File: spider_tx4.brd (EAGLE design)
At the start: 15.4 x 30.5 mm, 6 parts, among them J1 AVR_SPI_PRG_6NS

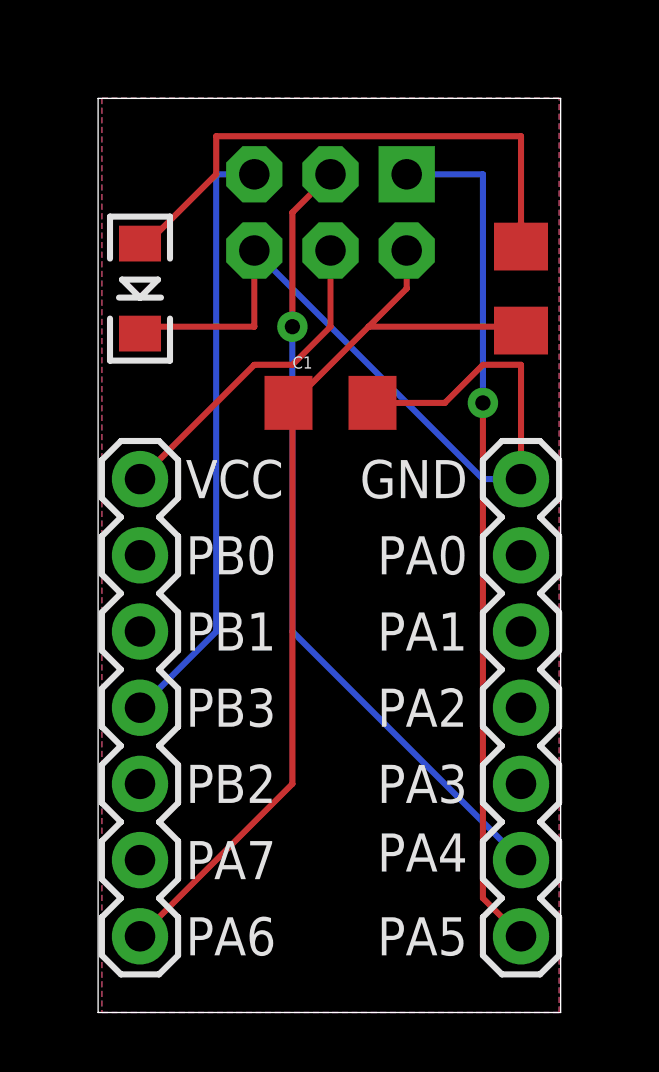
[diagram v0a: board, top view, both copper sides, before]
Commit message: noticed bug in board spidertx4.  fixed.  still tweaking.
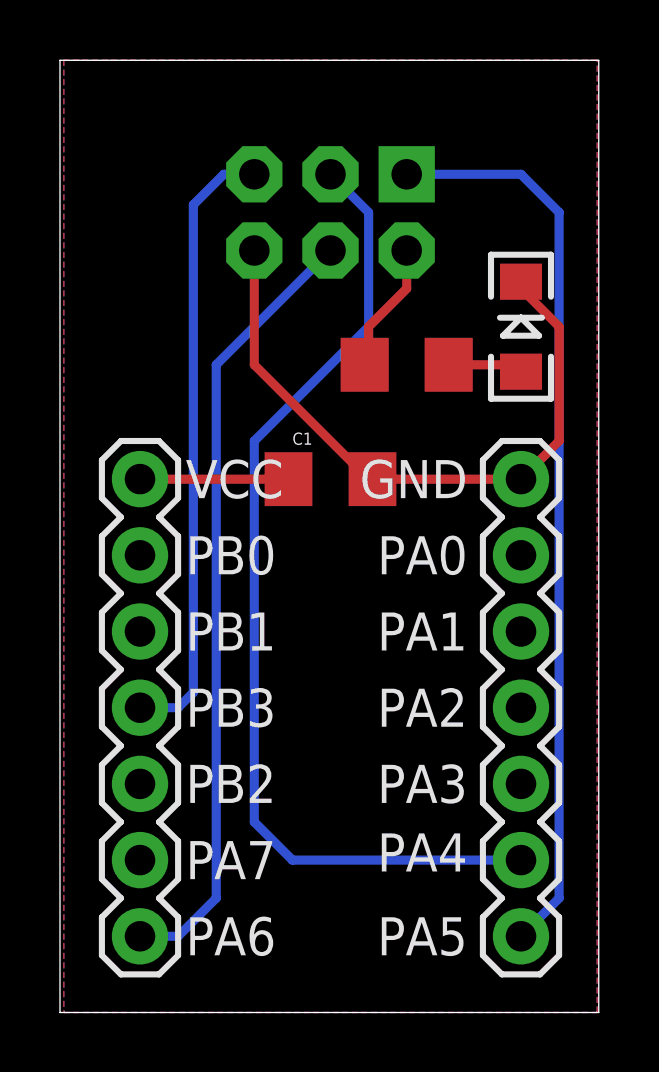
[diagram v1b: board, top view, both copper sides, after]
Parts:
- moved LEFT 15.2 mm to (2.54, 2.54), turned to 90 degrees
- moved D1 12.8 mm to (15.2, 22.9), turned to 90 degrees
- moved R1 4.58 mm to (11.4, 21.6), turned to 0 degrees
- moved C1 2.54 mm to (8.89, 17.8)
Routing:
- net VCC: track 31.9 -> 9.62 mm
- net N$14: track 19.1 -> 2.51 mm
- net MOSI: track 11.0 -> 26.2 mm
- net SCK: track 26.5 -> 33.1 mm, vias 1 -> 0
- net GND: track 28.0 -> 21.9 mm
- net MISO: track 28.5 -> 30.3 mm, vias 1 -> 0
- net RESET: track 20.1 -> 20.7 mm
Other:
- board size 15.4 x 30.5 mm -> 18 x 31.7 mm

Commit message: tweaked tx4 spider to death.  printing and testing.
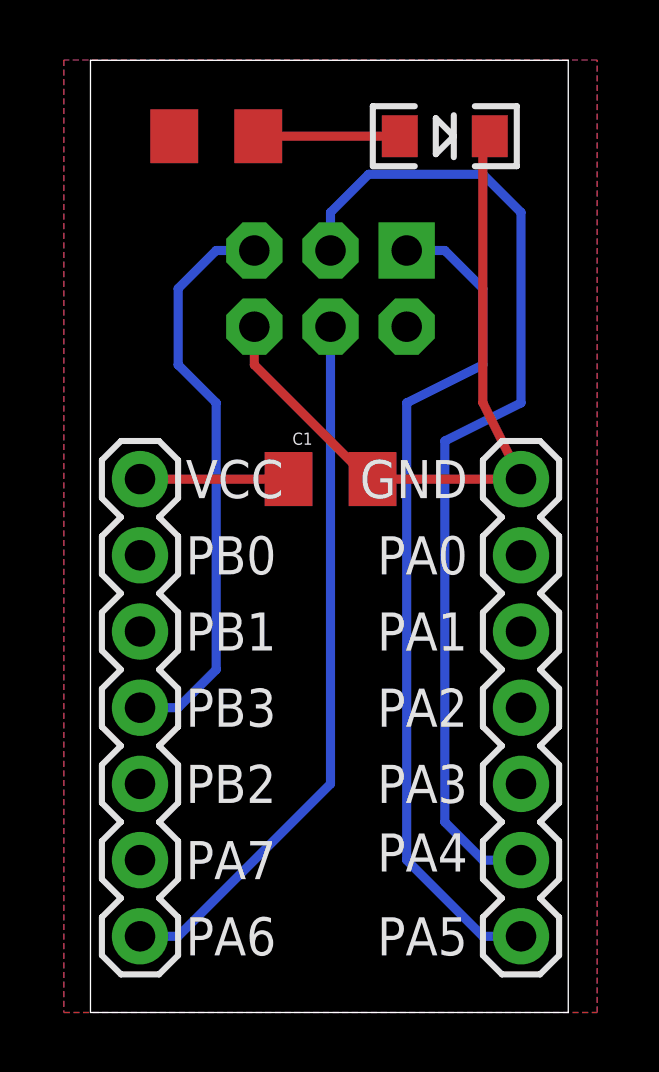
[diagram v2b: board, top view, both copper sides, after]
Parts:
- moved R1 9.92 mm to (5.08, 29.2)
- moved D1 6.84 mm to (12.7, 29.2), turned to 0 degrees
- moved J1 2.54 mm to (8.89, 24.1)
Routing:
- net VCC: track 9.62 -> 4.95 mm
- net N$14: track 2.51 -> 5.08 mm
- net MOSI: track 26.2 -> 23.7 mm
- net GND: track 21.9 -> 23.7 mm
- net MISO: track 30.3 -> 28.5 mm
- net RESET: track 20.7 -> 19.4 mm
- net SCK: track 33.1 -> 33.6 mm
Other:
- board size 18 x 31.7 mm -> 15.9 x 31.7 mm
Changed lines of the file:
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@@
 <board>
 <plain>
-<wire x1="-0.127" y1="0" x2="17.831" y2="0" width="0" layer="20"/>
-<wire x1="17.831" y1="0" x2="17.831" y2="31.74" width="0" layer="20"/>
-<wire x1="17.831" y1="31.74" x2="-0.127" y2="31.74" width="0" layer="20"/>
-<wire x1="-0.127" y1="31.74" x2="-0.127" y2="0" width="0" layer="20"/>
+<wire x1="0.889" y1="0" x2="16.815" y2="0" width="0" layer="20"/>
+<wire x1="16.815" y1="0" x2="16.815" y2="31.74" width="0" layer="20"/>
+<wire x1="16.815" y1="31.74" x2="0.889" y2="31.74" width="0" layer="20"/>
+<wire x1="0.889" y1="31.74" x2="0.889" y2="0" width="0" layer="20"/>
 <text x="13.462" y="17.78" size="1.27" layer="25" align="center-right">GND</text>
 <text x="13.462" y="15.24" size="1.27" layer="25" align="center-right">PA0</text>
@@
 </autorouter>
 <elements>
-<element name="J1" library="SparkFun-Connectors" package="2X3-NS" value="AVR_SPI_PRG_6NS" x="8.89" y="26.67" smashed="yes" rot="R180"/>
-<element name="R1" library="SparkFun-Passives" package="1206" value="1k Ohm" x="11.43" y="21.59" smashed="yes">
-<attribute name="VALUE" x="10.541" y="23.114" size="0.4064" layer="27"/>
+<element name="J1" library="SparkFun-Connectors" package="2X3-NS" value="AVR_SPI_PRG_6NS" x="8.89" y="24.13" smashed="yes" rot="R180"/>
+<element name="R1" library="SparkFun-Passives" package="1206" value="1k Ohm" x="5.08" y="29.21" smashed="yes">
+<attribute name="VALUE" x="4.191" y="30.734" size="0.4064" layer="27"/>
 </element>
-<element name="D1" library="SparkFun-LED" package="LED-1206" value="Yellow" x="15.24" y="22.86" smashed="yes" rot="R90">
-<attribute name="PROD_ID" value="DIO-09909" x="38.1" y="38.1" size="1.778" layer="27" rot="R90" display="off"/>
-<attribute name="VALUE" x="13.716" y="22.098" size="0.4064" layer="27" rot="R90"/>
+<element name="D1" library="SparkFun-LED" package="LED-1206" value="Yellow" x="12.7" y="29.21" smashed="yes">
+<attribute name="PROD_ID" value="DIO-09909" x="27.94" y="6.35" size="1.778" layer="27" display="off"/>
+<attribute name="VALUE" x="11.938" y="30.734" size="0.4064" layer="27"/>
 </element>
 <element name="C1" library="SparkFun-Passives" package="1206" value="0.1uF" x="8.89" y="17.78"/>
@@
 <contactref element="J1" pad="3"/>
 <contactref element="RIGHT" pad="6"/>
-<wire x1="8.89" y1="27.94" x2="10.16" y2="26.67" width="0.3048" layer="16"/>
-<wire x1="10.16" y1="26.67" x2="10.16" y2="22.86" width="0.3048" layer="16"/>
-<wire x1="10.16" y1="22.86" x2="6.35" y2="19.05" width="0.3048" layer="16"/>
-<wire x1="6.35" y1="19.05" x2="6.35" y2="6.35" width="0.3048" layer="16"/>
-<wire x1="6.35" y1="6.35" x2="7.62" y2="5.08" width="0.3048" layer="16"/>
-<wire x1="7.62" y1="5.08" x2="15.24" y2="5.08" width="0.3048" layer="16"/>
+<wire x1="13.97" y1="5.08" x2="15.24" y2="5.08" width="0.3048" layer="16"/>
+<wire x1="8.89" y1="25.4" x2="8.89" y2="26.67" width="0.3048" layer="16"/>
+<wire x1="8.89" y1="26.67" x2="10.16" y2="27.94" width="0.3048" layer="16"/>
+<wire x1="10.16" y1="27.94" x2="13.97" y2="27.94" width="0.3048" layer="16"/>
+<wire x1="13.97" y1="27.94" x2="15.24" y2="26.67" width="0.3048" layer="16"/>
+<wire x1="15.24" y1="26.67" x2="15.24" y2="20.32" width="0.3048" layer="16"/>
+<wire x1="15.24" y1="20.32" x2="12.7" y2="19.05" width="0.3048" layer="16"/>
+<wire x1="12.7" y1="19.05" x2="12.7" y2="6.35" width="0.3048" layer="16"/>
+<wire x1="12.7" y1="6.35" x2="13.97" y2="5.08" width="0.3048" layer="16"/>
 </signal>
 <signal name="MISO">
 <contactref element="J1" pad="1"/>
 <contactref element="RIGHT" pad="7"/>
-<wire x1="15.24" y1="2.54" x2="16.51" y2="3.81" width="0.3048" layer="16"/>
-<wire x1="16.51" y1="3.81" x2="16.51" y2="26.67" width="0.3048" layer="16"/>
-<wire x1="16.51" y1="26.67" x2="15.24" y2="27.94" width="0.3048" layer="16"/>
-<wire x1="15.24" y1="27.94" x2="11.43" y2="27.94" width="0.3048" layer="16"/>
+<wire x1="13.97" y1="2.54" x2="15.24" y2="2.54" width="0.3048" layer="16"/>
+<wire x1="11.43" y1="5.08" x2="13.97" y2="2.54" width="0.3048" layer="16"/>
+<wire x1="11.43" y1="20.32" x2="11.43" y2="5.08" width="0.3048" layer="16"/>
+<wire x1="13.97" y1="21.59" x2="11.43" y2="20.32" width="0.3048" layer="16"/>
+<wire x1="13.97" y1="21.59" x2="13.97" y2="24.13" width="0.3048" layer="16"/>
+<wire x1="13.97" y1="24.13" x2="12.7" y2="25.4" width="0.3048" layer="16"/>
+<wire x1="12.7" y1="25.4" x2="11.43" y2="25.4" width="0.3048" layer="16"/>
 </signal>
 <signal name="MOSI">
 <contactref element="J1" pad="4"/>
 <contactref element="LEFT" pad="1"/>
-<wire x1="8.89" y1="25.4" x2="5.08" y2="21.59" width="0.3048" layer="16"/>
-<wire x1="5.08" y1="21.59" x2="5.08" y2="3.81" width="0.3048" layer="16"/>
-<wire x1="5.08" y1="3.81" x2="3.81" y2="2.54" width="0.3048" layer="16"/>
 <wire x1="3.81" y1="2.54" x2="2.54" y2="2.54" width="0.3048" layer="16"/>
+<wire x1="8.89" y1="7.62" x2="3.81" y2="2.54" width="0.3048" layer="16"/>
+<wire x1="8.89" y1="22.86" x2="8.89" y2="7.62" width="0.3048" layer="16"/>
 </signal>
 <signal name="RESET">
 <contactref element="J1" pad="5"/>
 <contactref element="LEFT" pad="4"/>
-<wire x1="6.35" y1="27.94" x2="5.334" y2="27.94" width="0.3048" layer="16"/>
-<wire x1="5.334" y1="27.94" x2="4.318" y2="26.924" width="0.3048" layer="16"/>
-<wire x1="4.318" y1="26.924" x2="4.318" y2="10.668" width="0.3048" layer="16"/>
-<wire x1="4.318" y1="10.668" x2="3.81" y2="10.16" width="0.3048" layer="16"/>
 <wire x1="3.81" y1="10.16" x2="2.54" y2="10.16" width="0.3048" layer="16"/>
+<wire x1="5.08" y1="11.43" x2="3.81" y2="10.16" width="0.3048" layer="16"/>
+<wire x1="5.08" y1="20.32" x2="5.08" y2="11.43" width="0.3048" layer="16"/>
+<wire x1="5.08" y1="25.4" x2="3.81" y2="24.13" width="0.3048" layer="16"/>
+<wire x1="6.35" y1="25.4" x2="5.08" y2="25.4" width="0.3048" layer="16"/>
+<wire x1="3.81" y1="24.13" x2="3.81" y2="21.59" width="0.3048" layer="16"/>
+<wire x1="3.81" y1="21.59" x2="5.08" y2="20.32" width="0.3048" layer="16"/>
 </signal>
 <signal name="VCC">
@@
 <contactref element="LEFT" pad="7"/>
 <wire x1="2.54" y1="17.78" x2="7.49" y2="17.78" width="0.3048" layer="1"/>
-<wire x1="11.43" y1="25.4" x2="11.43" y2="24.13" width="0.3048" layer="1"/>
-<wire x1="11.43" y1="24.13" x2="10.16" y2="22.86" width="0.3048" layer="1"/>
-<wire x1="10.16" y1="22.86" x2="10.16" y2="21.72" width="0.3048" layer="1"/>
-<wire x1="10.16" y1="21.72" x2="10.03" y2="21.59" width="0.3048" layer="1"/>
 <polygon width="0.3048" layer="1">
 <vertex x="0" y="31.75"/>
@@
 <vertex x="17.78" y="31.75"/>
 </polygon>
-<wire x1="10.16" y1="21.59" x2="10.03" y2="21.59" width="0.3048" layer="1"/>
-<wire x1="10.16" y1="21.59" x2="10.182390625" y2="21.742409375" width="0.3048" layer="1"/>
 </signal>
 <signal name="GND">
@@
 </polygon>
 <wire x1="15.24" y1="17.78" x2="10.29" y2="17.78" width="0.3048" layer="1"/>
-<wire x1="6.35" y1="25.4" x2="6.35" y2="21.59" width="0.3048" layer="1"/>
+<wire x1="6.35" y1="22.86" x2="6.35" y2="21.59" width="0.3048" layer="1"/>
 <wire x1="6.35" y1="21.59" x2="10.16" y2="17.78" width="0.3048" layer="1"/>
 <wire x1="10.16" y1="17.78" x2="10.29" y2="17.78" width="0.3048" layer="1"/>
-<wire x1="16.51" y1="22.86" x2="15.24" y2="24.13" width="0.3048" layer="1"/>
-<wire x1="16.51" y1="19.05" x2="16.51" y2="22.86" width="0.3048" layer="1"/>
-<wire x1="15.24" y1="17.78" x2="16.51" y2="19.05" width="0.3048" layer="1"/>
-<wire x1="15.24" y1="24.13" x2="15.24" y2="24.36" width="0.3048" layer="1"/>
+<wire x1="13.97" y1="20.32" x2="13.97" y2="29.21" width="0.3048" layer="1"/>
+<wire x1="15.24" y1="17.78" x2="13.97" y2="20.32" width="0.3048" layer="1"/>
+<wire x1="13.97" y1="29.21" x2="14.2" y2="29.21" width="0.3048" layer="1"/>
 </signal>
 <signal name="N$14">
 <contactref element="R1" pad="2"/>
 <contactref element="D1" pad="A"/>
-<wire x1="12.83" y1="21.59" x2="15.01" y2="21.59" width="0.3048" layer="1"/>
-<wire x1="15.01" y1="21.59" x2="15.24" y2="21.36" width="0.3048" layer="1"/>
+<wire x1="6.48" y1="29.21" x2="11.2" y2="29.21" width="0.3048" layer="1"/>
+<wire x1="11.43" y1="29.21" x2="11.2" y2="29.21" width="0.3048" layer="1"/>
+<wire x1="6.35" y1="29.21" x2="6.48" y2="29.21" width="0.3048" layer="1"/>
 </signal>
 </signals>
